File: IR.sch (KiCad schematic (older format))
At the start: 6 parts

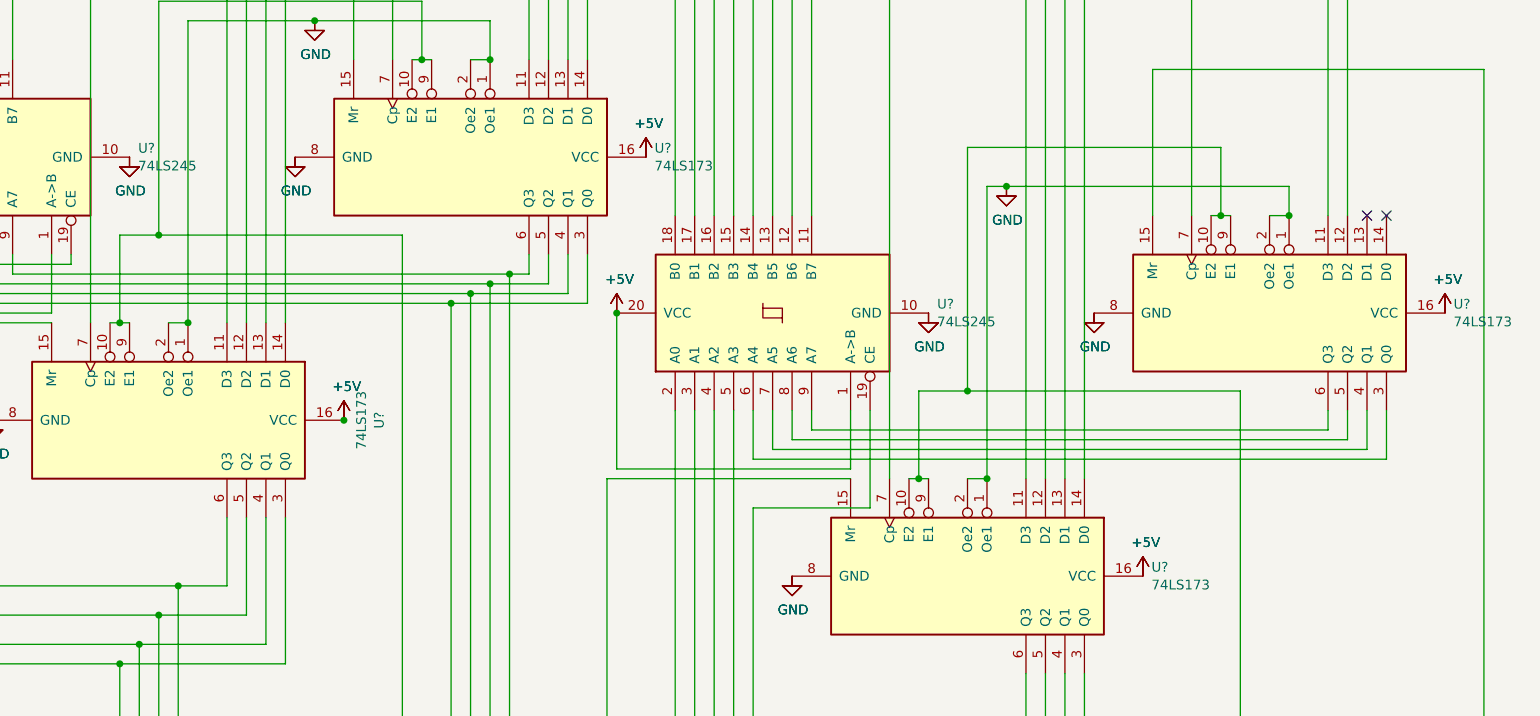
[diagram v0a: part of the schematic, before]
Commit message: Fixed power for multi part comps
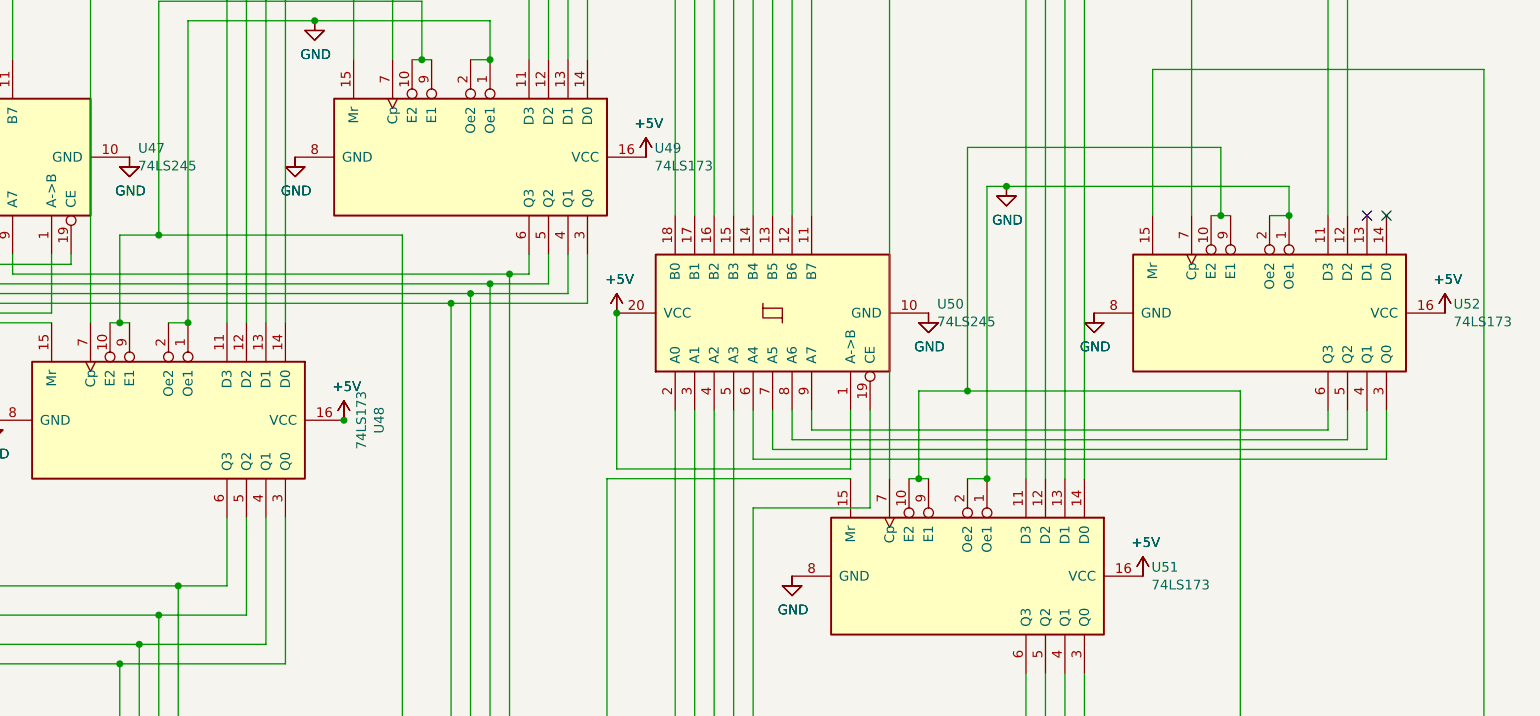
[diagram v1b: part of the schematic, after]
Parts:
- gave numbers to parts that had none: 6

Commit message: Fixed ZIF
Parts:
- U47, U50: symbol 74xx:74LS245 -> 16bitCpu-rescue:74LS245-74xx
- U48, U49, U51, U52: symbol 74xx:74LS173 -> 16bitCpu-rescue:74LS173-74xx
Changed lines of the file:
@@
 	8750 6550 8750 7200
 $Comp
-L power:GND #PWR?
+L 16bitCpu-rescue:GND-power #PWR?
 U 1 1 5F7C1DC5
 P 8050 4700
@@
 $EndComp
 $Comp
-L power:GND #PWR?
+L 16bitCpu-rescue:GND-power #PWR?
 U 1 1 5F7C1DCB
 P 8900 4700
@@
 $EndComp
 $Comp
-L power:GND #PWR?
+L 16bitCpu-rescue:GND-power #PWR?
 U 1 1 5F7C1DD1
 P 7350 6050
@@
 $EndComp
 $Comp
-L power:GND #PWR?
+L 16bitCpu-rescue:GND-power #PWR?
 U 1 1 5F7C1DD7
 P 3250 5250
@@
 $EndComp
 $Comp
-L power:GND #PWR?
+L 16bitCpu-rescue:GND-power #PWR?
 U 1 1 5F7C1DDD
 P 3950 3900
@@
 $EndComp
 $Comp
-L power:GND #PWR?
+L 16bitCpu-rescue:GND-power #PWR?
 U 1 1 5F7C1DE3
 P 4800 3900
@@
 $EndComp
 $Comp
-L power:+5V #PWR?
+L 16bitCpu-rescue:+5V-power #PWR?
 U 1 1 5F7C1DE9
 P 5050 5250
@@
 $EndComp
 $Comp
-L power:+5V #PWR?
+L 16bitCpu-rescue:+5V-power #PWR?
 U 1 1 5F7C1DEF
 P 6450 4700
@@
 $EndComp
 $Comp
-L power:+5V #PWR?
+L 16bitCpu-rescue:+5V-power #PWR?
 U 1 1 5F7C1DF5
 P 9150 6050
@@
 $EndComp
 $Comp
-L power:+5V #PWR?
+L 16bitCpu-rescue:+5V-power #PWR?
 U 1 1 5F7C1DFB
 P 10700 4700
@@
 $EndComp
 $Comp
-L power:+5V #PWR?
+L 16bitCpu-rescue:+5V-power #PWR?
 U 1 1 5F7C1E01
 P 6600 3900
@@
 Connection ~ 5800 3400
 $Comp
-L power:GND #PWR?
+L 16bitCpu-rescue:GND-power #PWR?
 U 1 1 5F7C1E0D
 P 4900 3200
@@
 Connection ~ 9900 4200
 $Comp
-L power:GND #PWR?
+L 16bitCpu-rescue:GND-power #PWR?
 U 1 1 5F7C1E1C
 P 8450 4050
@@
 Bus12
 $Comp
-L 74xx:74LS173 U?
+L 16bitCpu-rescue:74LS173-74xx U?
 U 1 1 5F7C1E87
 P 4150 5250
@@
 $EndComp
 $Comp
-L 74xx:74LS245 U?
+L 16bitCpu-rescue:74LS245-74xx U?
 U 1 1 5F7C1E8D
 P 3150 3900
@@
 $EndComp
 $Comp
-L 74xx:74LS173 U?
+L 16bitCpu-rescue:74LS173-74xx U?
 U 1 1 5F7C1E93
 P 9800 4700
@@
 $EndComp
 $Comp
-L power:GND #PWR?
+L 16bitCpu-rescue:GND-power #PWR?
 U 1 1 5F7C1E99
 P 8050 4700
@@
 $EndComp
 $Comp
-L power:GND #PWR?
+L 16bitCpu-rescue:GND-power #PWR?
 U 1 1 5F7C1E9F
 P 8900 4700
@@
 $EndComp
 $Comp
-L power:GND #PWR?
+L 16bitCpu-rescue:GND-power #PWR?
 U 1 1 5F7C1EA5
 P 7350 6050
@@
 $EndComp
 $Comp
-L power:GND #PWR?
+L 16bitCpu-rescue:GND-power #PWR?
 U 1 1 5F7C1EAB
 P 3250 5250
@@
 $EndComp
 $Comp
-L power:GND #PWR?
+L 16bitCpu-rescue:GND-power #PWR?
 U 1 1 5F7C1EB1
 P 3950 3900
@@
 $EndComp
 $Comp
-L power:GND #PWR?
+L 16bitCpu-rescue:GND-power #PWR?
 U 1 1 5F7C1EB7
 P 4800 3900
@@
 $EndComp
 $Comp
-L power:+5V #PWR?
+L 16bitCpu-rescue:+5V-power #PWR?
 U 1 1 5F7C1EBD
 P 2350 3900
@@
 $EndComp
 $Comp
-L power:+5V #PWR?
+L 16bitCpu-rescue:+5V-power #PWR?
 U 1 1 5F7C1EC3
 P 5050 5250
@@
 $EndComp
 $Comp
-L power:+5V #PWR?
+L 16bitCpu-rescue:+5V-power #PWR?
 U 1 1 5F7C1EC9
 P 6450 4700
@@
 $EndComp
 $Comp
-L power:+5V #PWR?
+L 16bitCpu-rescue:+5V-power #PWR?
 U 1 1 5F7C1ECF
 P 9150 6050
@@
 $EndComp
 $Comp
-L power:+5V #PWR?
+L 16bitCpu-rescue:+5V-power #PWR?
 U 1 1 5F7C1ED5
 P 10700 4700
@@
 $EndComp
 $Comp
-L power:+5V #PWR?
+L 16bitCpu-rescue:+5V-power #PWR?
 U 1 1 5F7C1EDB
 P 6600 3900
@@
 $EndComp
 $Comp
-L power:GND #PWR?
+L 16bitCpu-rescue:GND-power #PWR?
 U 1 1 5F7C1EE1
 P 4900 3200
@@
 $EndComp
 $Comp
-L power:GND #PWR?
+L 16bitCpu-rescue:GND-power #PWR?
 U 1 1 5F7C1EE7
 P 8450 4050
@@
 	10900 3450 10900 8150
 $Comp
-L 74xx:74LS173 U?
+L 16bitCpu-rescue:74LS173-74xx U?
 U 1 1 5F7C1F02
 P 8250 6050
@@
 $EndComp
 $Comp
-L 74xx:74LS173 U?
+L 16bitCpu-rescue:74LS173-74xx U?
 U 1 1 5F7C1F08
 P 5700 3900
@@
 	5350 4300 5350 8500
 $Comp
-L 74xx:74LS245 U?
+L 16bitCpu-rescue:74LS245-74xx U?
 U 1 1 5F7C1F10
 P 7250 4700
@@
 ~II
 $Comp
-L power:+5V #PWR?
+L 16bitCpu-rescue:+5V-power #PWR?
 U 1 1 5F7C1F7F
 P 2350 3900

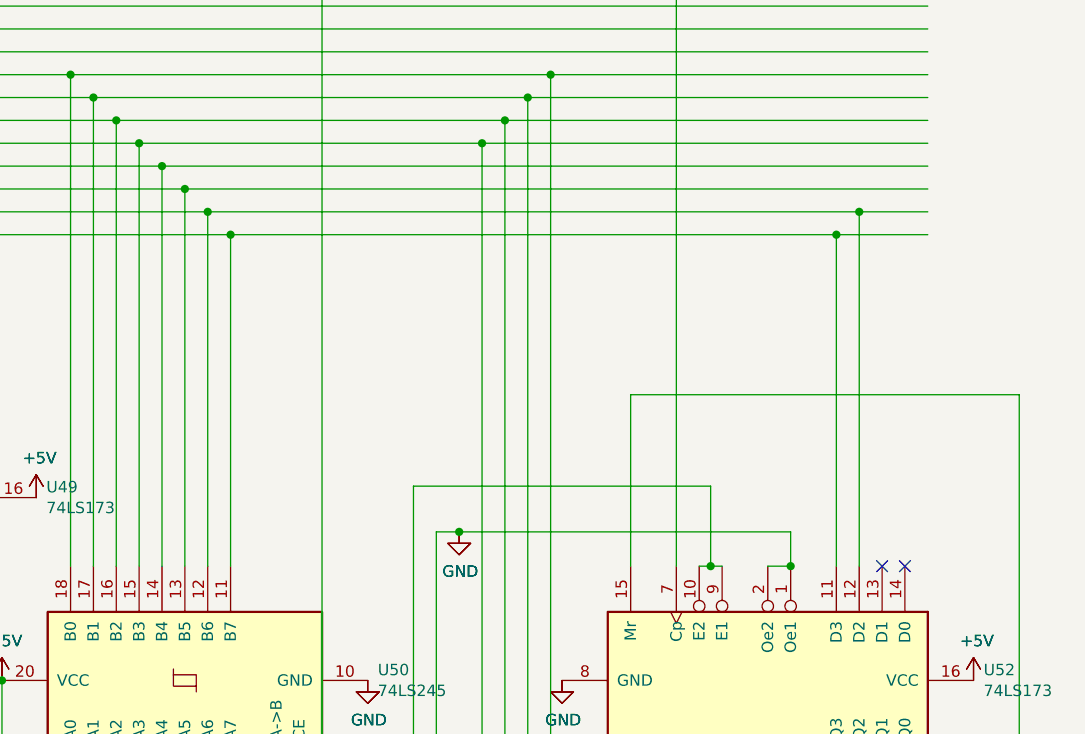
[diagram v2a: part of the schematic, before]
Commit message: changed ir to only hold 12
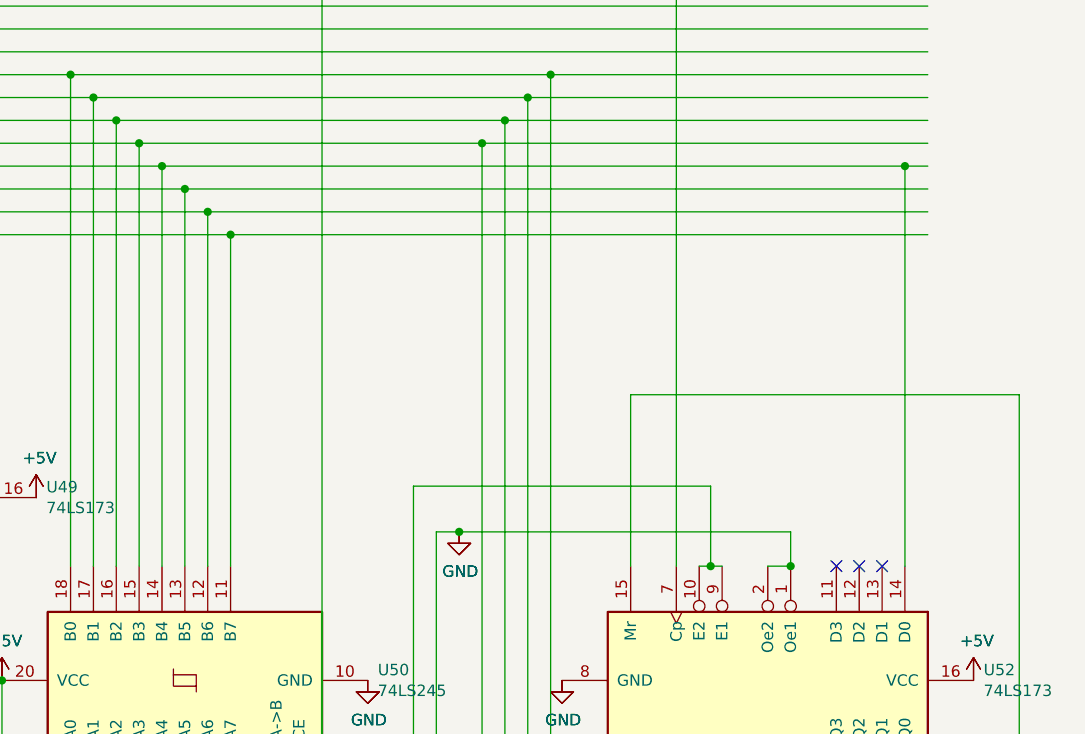
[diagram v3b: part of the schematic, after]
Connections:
- wire segments 215 -> 213
- no-connect marks 2 -> 3
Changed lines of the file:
@@
 	8650 5550 8650 2250
-Wire Wire Line
-	10200 4200 10200 2650
-Wire Wire Line
-	10100 4200 10100 2750
 Wire Wire Line
 	8850 7300 8850 6550
@@
 Connection ~ 7350 2650
 Wire Wire Line
-	7350 2650 10200 2650
-Wire Wire Line
 	7450 4200 7450 2750
 Connection ~ 7450 2750
-Wire Wire Line
-	7450 2750 10100 2750
 Connection ~ 8550 2350
 Wire Wire Line
@@
 Wire Wire Line
 	8850 2050 10500 2050
-Connection ~ 10100 2750
-Wire Wire Line
-	10100 2750 10500 2750
-Connection ~ 10200 2650
-Wire Wire Line
-	10200 2650 10500 2650
 Wire Wire Line
 	8750 6550 8750 7200
@@
 	7350 5350 10200 5350
 Wire Wire Line
-	7150 2450 10500 2450
+	7150 2450 10400 2450
 Wire Wire Line
 	7250 2550 10500 2550
-NoConn ~ 10400 4200
+Wire Wire Line
+	1950 1550 2950 1550
+Wire Wire Line
+	7450 2750 10500 2750
+Wire Wire Line
+	7350 2650 10500 2650
+Wire Wire Line
+	10400 4200 10400 2450
+Connection ~ 10400 2450
+Wire Wire Line
+	10400 2450 10500 2450
 NoConn ~ 10300 4200
-Wire Wire Line
-	1950 1550 2950 1550
+NoConn ~ 10200 4200
+NoConn ~ 10100 4200
 $EndSCHEMATC

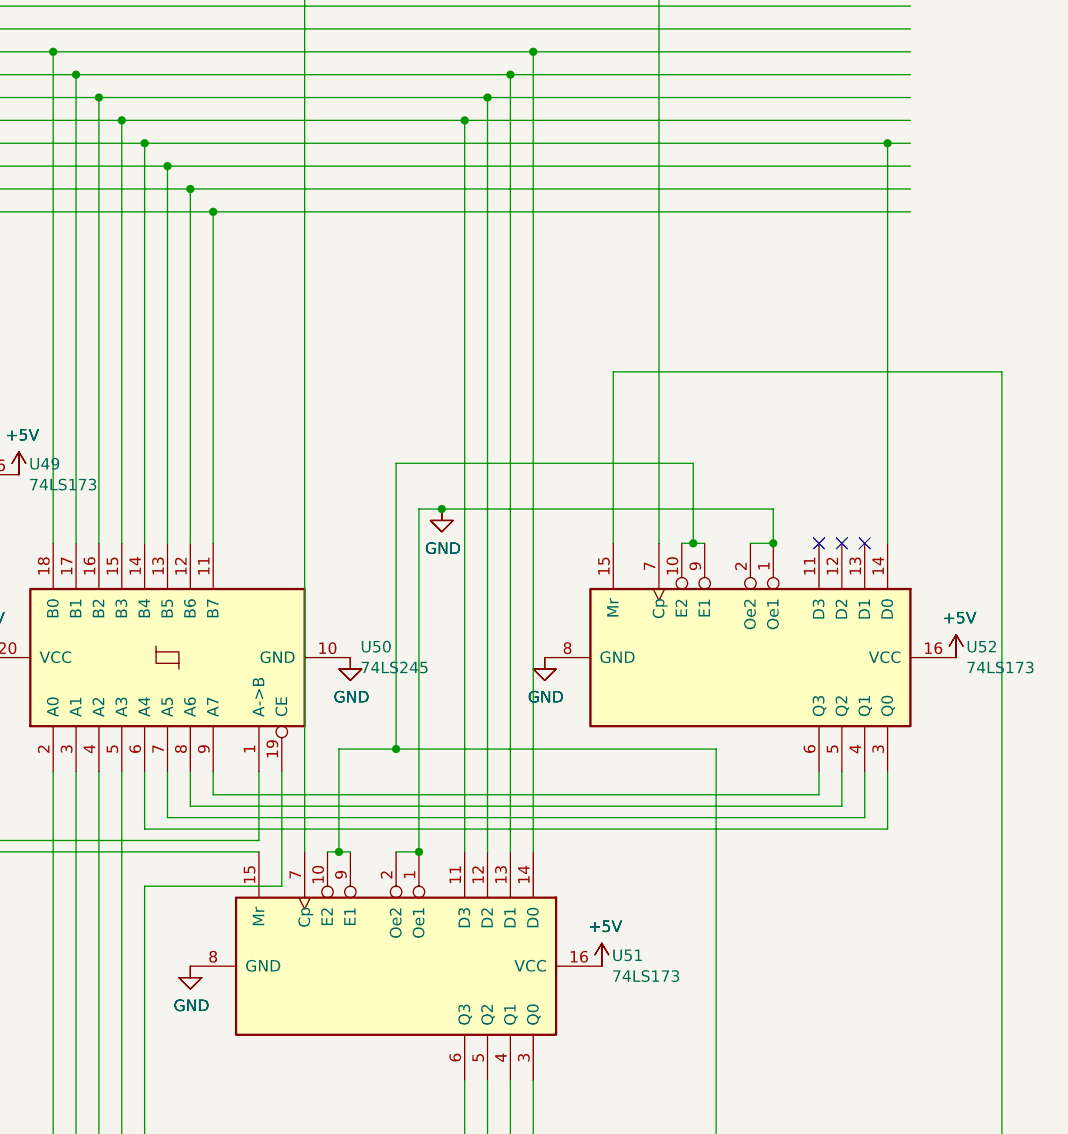
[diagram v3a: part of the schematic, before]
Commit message: non floating ram and ir , added stack register
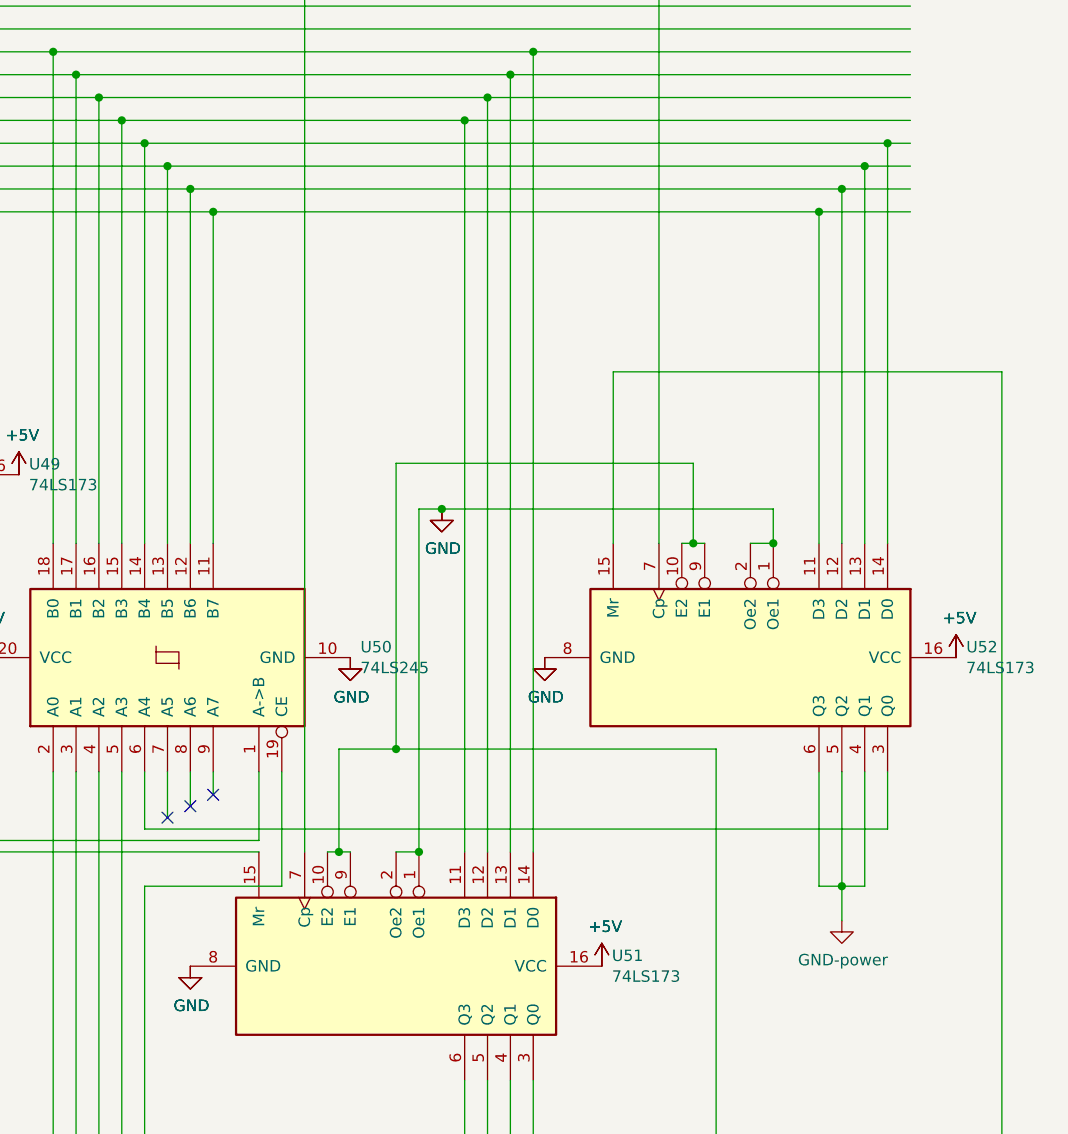
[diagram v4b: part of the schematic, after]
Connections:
- net labels added: GND-power
- wire segments 213 -> 219
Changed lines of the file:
@@
 $Descr A3 16535 11693
 encoding utf-8
-Sheet 8 9
+Sheet 8 10
 Title ""
 Date ""
@@
 	7250 5200 7250 5400
 Wire Wire Line
-	10300 5400 10300 5200
-Wire Wire Line
-	10200 5200 10200 5350
-Wire Wire Line
 	7350 5350 7350 5200
 Wire Wire Line
 	7450 5200 7450 5300
 Wire Wire Line
-	10100 5300 10100 5200
-Wire Wire Line
 	8550 5550 8550 2350
-Wire Wire Line
-	7450 5300 10100 5300
 Connection ~ 6750 2050
 Wire Wire Line
@@
 	7150 5450 10400 5450
 Wire Wire Line
-	7250 5400 10300 5400
-Wire Wire Line
-	7350 5350 10200 5350
-Wire Wire Line
 	7150 2450 10400 2450
 Wire Wire Line
-	7250 2550 10500 2550
+	7250 2550 10300 2550
 Wire Wire Line
 	1950 1550 2950 1550
 Wire Wire Line
-	7450 2750 10500 2750
-Wire Wire Line
-	7350 2650 10500 2650
+	7450 2750 10100 2750
+Wire Wire Line
+	7350 2650 10200 2650
 Wire Wire Line
 	10400 4200 10400 2450
@@
 Wire Wire Line
 	10400 2450 10500 2450
-NoConn ~ 10300 4200
-NoConn ~ 10200 4200
-NoConn ~ 10100 4200
+Wire Wire Line
+	10100 5700 10200 5700
+Wire Wire Line
+	10200 5200 10200 5700
+Wire Wire Line
+	10100 5200 10100 5700
+Wire Wire Line
+	10300 5700 10200 5700
+Wire Wire Line
+	10300 5200 10300 5700
+Connection ~ 10200 5700
+Wire Wire Line
+	10200 5700 10200 5850
+$Comp
+L 16bitCpu-rescue:GND-power #PWR?
+U 1 1 60F44F5B
+P 10200 5850
+F 0 "#PWR?" H 10200 5600 50  0001 C CNN
+F 1 "GND-power" H 10205 5677 50  0000 C CNN
+F 2 "" H 10200 5850 50  0001 C CNN
+F 3 "" H 10200 5850 50  0001 C CNN
+	1    10200 5850
+	1    0    0    -1
+$EndComp
+Wire Wire Line
+	10300 2550 10300 4200
+Connection ~ 10300 2550
+Wire Wire Line
+	10300 2550 10500 2550
+Wire Wire Line
+	10200 4200 10200 2650
+Connection ~ 10200 2650
+Wire Wire Line
+	10200 2650 10500 2650
+Wire Wire Line
+	10100 4200 10100 2750
+Connection ~ 10100 2750
+Wire Wire Line
+	10100 2750 10500 2750
+NoConn ~ 7250 5400
+NoConn ~ 7350 5350
+NoConn ~ 7450 5300
 $EndSCHEMATC
